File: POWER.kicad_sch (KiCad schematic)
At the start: 12 parts, among them J21 Conn_01x02, SW4 SW_Wuerth_450301014042, U8 AMS1117-3.3

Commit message: gerber files
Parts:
- removed SW4: SW_Wuerth_450301014042, Button_Switch_SMD:SW_SPDT_PCM12, symbol Switch:SW_Wuerth_450301014042
- added SW4: SW_SPDT, Button_Switch_SMD:SW_SPDT_PCM12, symbol Switch:SW_SPDT
- C34, C35: LCSC Part # (none) -> C88697
- C36, C37: LCSC Part # (none) -> C13585
- D3, D4: LCSC Part # (none) -> C2480
- J21, U7: now not fitted
- L3: LCSC Part # (none) -> C436517
- U8: LCSC Part # (none) -> C2891839
- U9: LCSC Part # (none) -> C2469138
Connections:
- net BAT+: now also U7.1 (BAT+)
- net GND: now also SW4.2 (B)
- new net: SW4.3 (C), U7.11 (ENB)

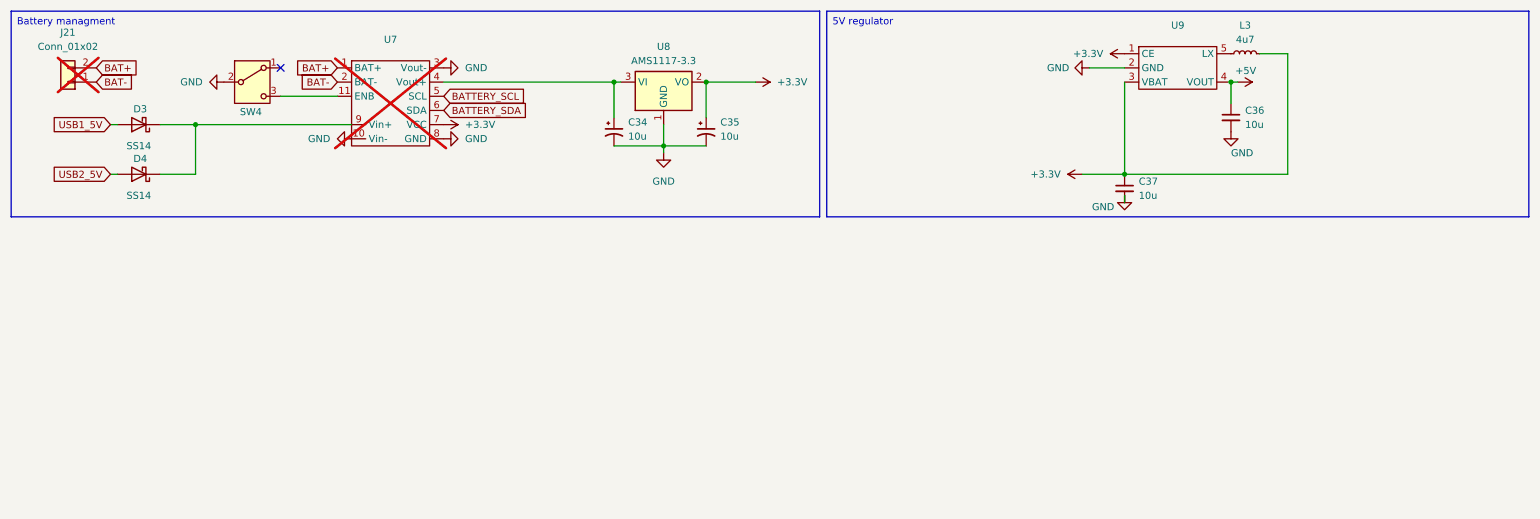
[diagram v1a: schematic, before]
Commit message: update to STM32F04
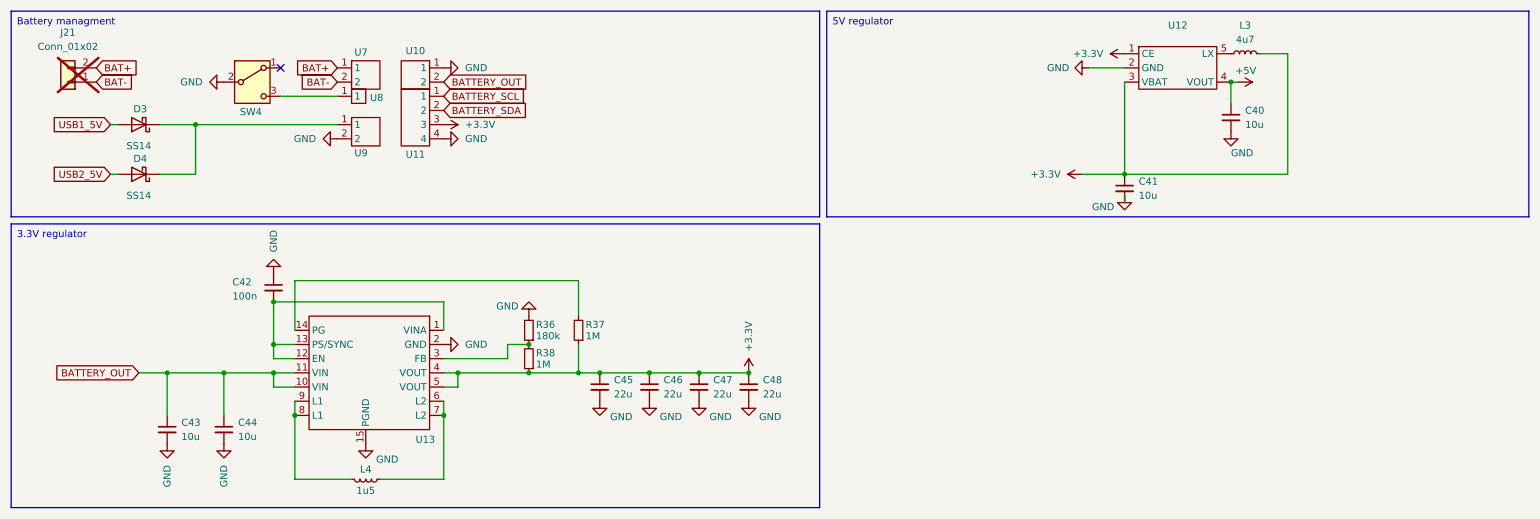
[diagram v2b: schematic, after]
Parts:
- removed C34, C35: 10u, Capacitor_SMD:C_Elec_10x10.2, symbol Device:C_Polarized_Small_US
- removed U7: ~, kwrzesni:BatteryBabysitter, symbol kwrzesni_symblos:BatteryBabysitter
- removed U8: AMS1117-3.3, Package_TO_SOT_SMD:SOT-223-3_TabPin2, symbol Regulator_Linear:AMS1117-3.3
- added C42: 100n, Capacitor_SMD:C_0402_1005Metric, symbol Device:C_Small
- added C43, C44: 10u, Capacitor_SMD:C_0603_1608Metric, symbol Device:C_Small
- added C45, C46, C47, C48: 22u, Capacitor_SMD:C_0603_1608Metric, symbol Device:C_Small
- added L4: 1u5, Inductor_SMD:L_Vishay_IFSC-1515AH_4x4x1.8mm, symbol Device:L_Small
- added R36: 180k, Resistor_SMD:R_0603_1608Metric, symbol Device:R_Small
- added R37, R38: 1M, Resistor_SMD:R_0603_1608Metric, symbol Device:R_Small
- added U10, U7, U9: ~, kwrzesni:DZ254S-11-02-48, symbol kwrzesni:DZ254S-11-02-48
- added U11: ~, kwrzesni:X6511WVS-04H-C60D48R1, symbol kwrzesni:X6511WVS-04H-C60D48R1
- added U13: ~, kwrzesni:TPS63020DSJR, symbol kwrzesni:TPS63020DSJR
- added U8: ~, kwrzesni:X6511WVS-01H-C60D48R2, symbol kwrzesni:X6511WVS-01H-C60D48R2
- renumbered C36 to C40, C37 to C41, U9 to U12
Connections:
- net +3.3V: now also C45.1, C46.1, C47.1, C48.1, R37.1, R38.1, U11.3, U13.4 (VOUT), U13.5 (VOUT)
- net BAT+: now also U7.1
- net BAT-: now also U7.2
- net BATTERY_SCL: now also U11.1
- net BATTERY_SDA: now also U11.2
- net GND: now also C42.1, C43.2, C44.2, C45.2, C46.2, C47.2, C48.2, R36.2, U10.1, U11.4, U13.15 (PGND), U13.2 (GND), U9.2
- net at D3.1 (K), D4.1 (K): now also U9.1
- net at SW4.3 (C): now also U8.1
- new net: R36.1, R38.2, U13.3 (FB)
- new net: L4.1, U13.6 (L2), U13.7 (L2)
- new net: L4.2, U13.8 (L1), U13.9 (L1)
- new net: R37.2, U13.14 (PG)
- new net: C42.2, U13.1 (VINA), U13.12 (EN), U13.13 (PS/SYNC)
- new net BATTERY_OUT: C43.1, C44.1, U10.2, U13.10 (VIN), U13.11 (VIN)
